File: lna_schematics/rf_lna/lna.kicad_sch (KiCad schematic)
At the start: 31 parts, among them J4 Conn_01x02_Pin, J5 Conn_Coaxial_Small, J6 Conn_Coaxial_Small, U5 L78L05_SOT89, U6 BFP640, U7 BFP640, U8 BFP640

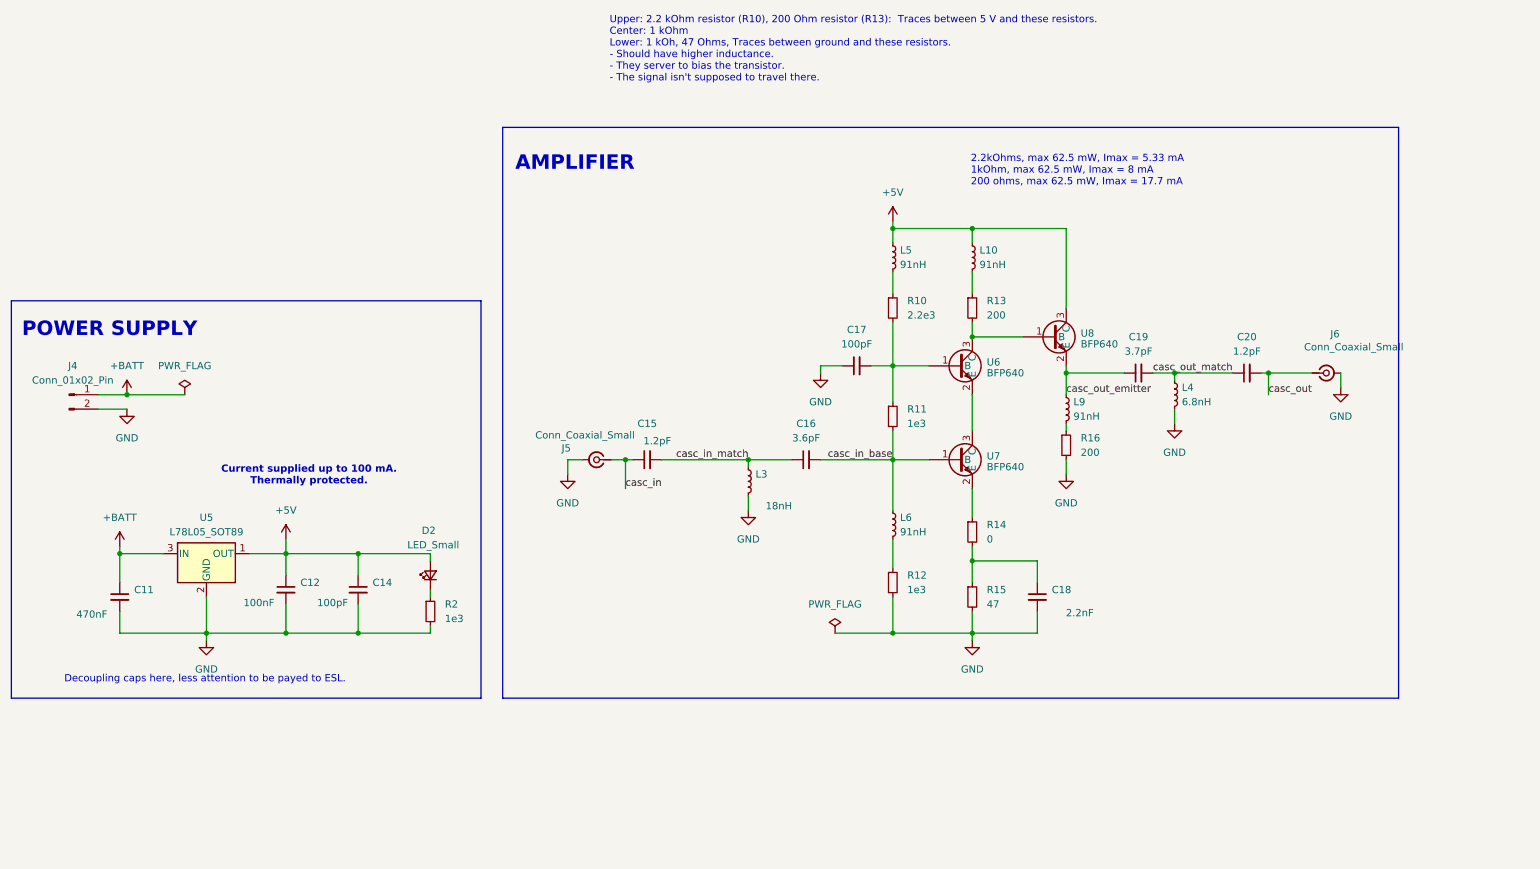
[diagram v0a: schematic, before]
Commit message: [lna_schematics] Added components for matching + inductances | TODO: place inductors to prevent capacitive coupling [simulations] Added stability factor and matching circuits | TODO: do bilateral matching for the SS-CC amp
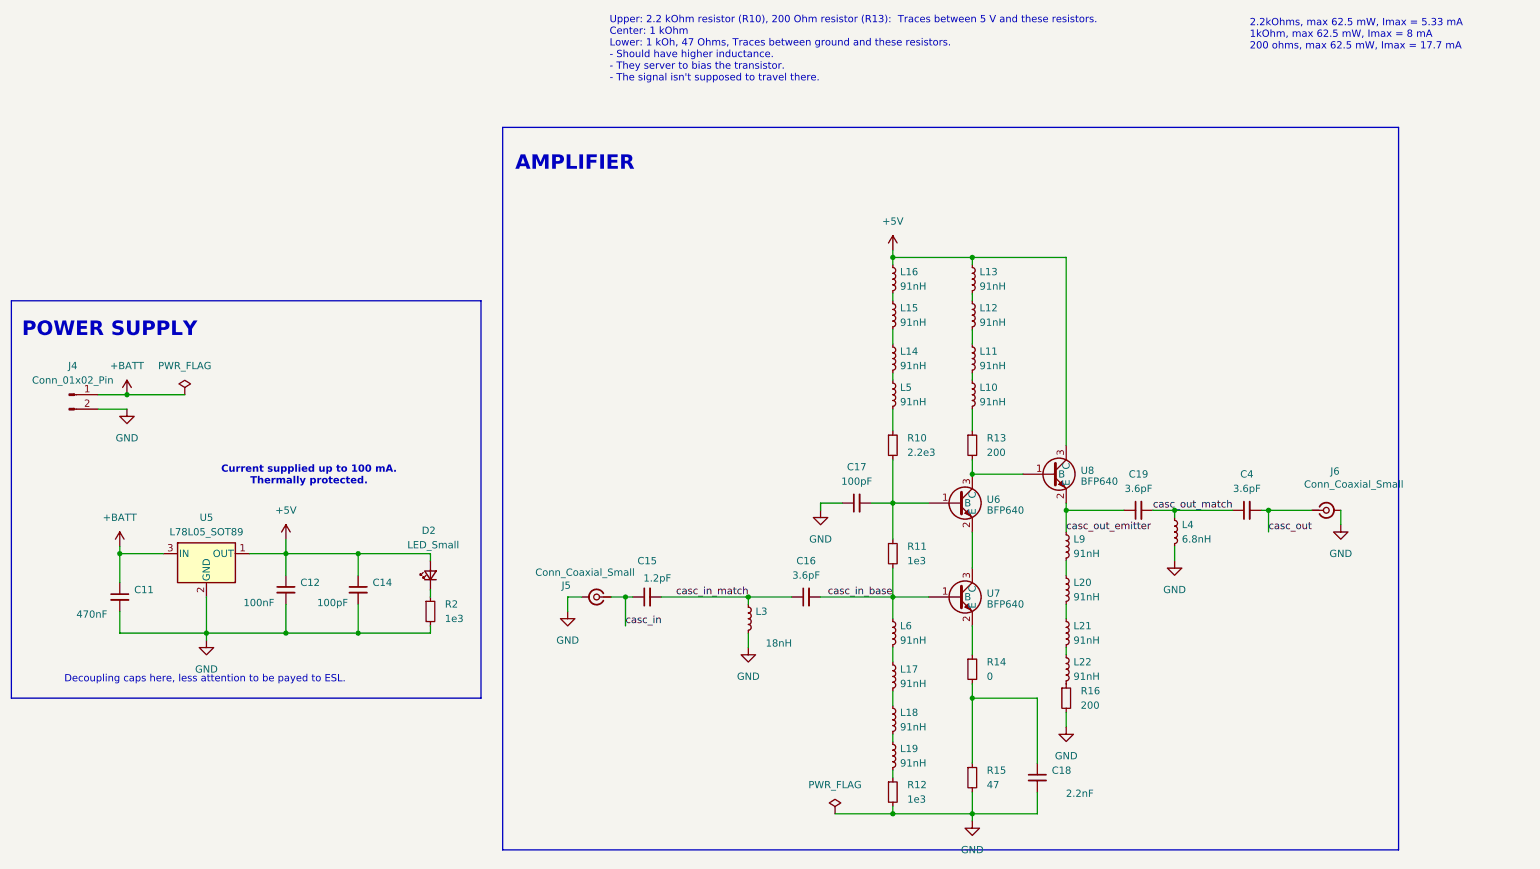
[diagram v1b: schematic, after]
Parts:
- removed C20: 1.2pF, Capacitor_SMD:C_0402_1005Metric, symbol Device:C_Small
- added C4: 3.6pF, Capacitor_SMD:C_0402_1005Metric, symbol Device:C_Small
- added L11, L12, L13, L14, L15, L16, L17, L18, L19, L20, L21, L22: 91nH, Inductor_SMD:L_0603_1608Metric, symbol Device:L_Small
- C19: value 3.7pF -> 3.6pF
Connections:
- net +5V: now also L13.1, L16.1; no longer L10.1, L5.1
- net casc_out: now also C4.2
- net casc_out_match: now also C4.1
- net at R16.1: now also L22.2; no longer L9.2
- net at L6.2: now also L17.1; no longer R12.1
- new net: L14.1, L15.2
- new net: L14.2, L5.1
- new net: L10.1, L11.2
- new net: L17.2, L18.1
- new net: L11.1, L12.2
- new net: L18.2, L19.1
- new net: L20.1, L9.2
- new net: L20.2, L21.1
- new net: L19.2, R12.1
- new net: L12.1, L13.2
- new net: L15.1, L16.2
- new net: L21.2, L22.1
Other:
- moved on the sheet: C15, C16, C17, C18, C19, J5, J6, L10, L3, L4, L5, L6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

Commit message: [rf_lna] did layout of rf amplifiers for LNA | TODO: create an antenna design for the bottom half
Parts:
- removed L10, L11, L14, L15, L16, L17, L18, L19, L20, L21, L22: 91nH, Inductor_SMD:L_0603_1608Metric, symbol Device:L_Small
- C15: value 1.2pF -> 1pF; LCSC Part Number C76899 -> C76953; Manufacturing Part Number GJM1555C1H1R2WB01D -> GRM1555C1H1R0CA01D
- L12, L13, L5, L6, L9: value 91nH -> 160nH; LCSC Part Number C237546 -> C140445; Manufacturing Part Number LQW18AN91NG0ZD -> LQW18ANR16J00D
- L3: value 18nH -> 20nH; LCSC Part Number C24562 -> C96730; Manufacturing Part Number SDCL1005C18NJTDF -> SDCL1005C20NJTDF
- L4: value 6.8nH -> 15nH; LCSC Part Number C32041 -> C27143; Manufacturing Part Number SDCL1005C6N8JTDF -> SDCL1005C15NJTDF
- R13, R16: LCSC Part Number C25091 -> C25087; Manufacturing Part Number 0402WGF2200TCE -> 0402WGF2000TCE
- R15: footprint Capacitor_SMD:C_0402_1005Metric -> Resistor_SMD:R_0603_1608Metric; LCSC Part Number C4109 -> C23182; Manufacturing Part Number 0402WGF2001TCE -> 0603WAF470JT5E
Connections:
- net +5V: now also L5.1
- net at R16.1: now also L9.2
- net at R13.1: now also L12.2
- net at L6.2: now also R12.1
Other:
- note added: "2-STAGE CASCODE"
- note removed: "AMPLIFIER"
- moved on the sheet: C18, L5, L6, L9, R12, R15, R16
